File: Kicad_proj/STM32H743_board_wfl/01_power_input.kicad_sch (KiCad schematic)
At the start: 5 parts

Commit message: v0.4 poprawki inputa zasilania
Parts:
- removed C6: 47uF, symbol Device:C
- removed C7: 1uF, symbol Device:C
- removed C8: 100nF, symbol Device:C
- removed L2: BLM21PG221SN1D, symbol Device:L_Ferrite
- added C1, C2: 47uF, Capacitor_SMD:C_1206_3216Metric, symbol Device:C
- added C3: 1uF, Capacitor_SMD:C_0603_1608Metric, symbol Device:C
- added C4: 100nF, Capacitor_SMD:C_01005_0402Metric, symbol Device:C
- added F2: 1A Fuse 0680L1000-05, STM32H743_board_library_footprints:FUSC6125X279N, symbol STM32H743_board_library_symbols:0680L1000-05
- D1: footprint (none) -> Diode_SMD:D_SMB
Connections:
- net +BATT: now also F2.1; no longer D1.2 (A2)
- net -BATT: now also C1.2, C2.2, C3.2, C4.2
- new net +26V_prefiltered: C1.1, C2.1, C3.1, C4.1, D1.2 (A2), F2.2

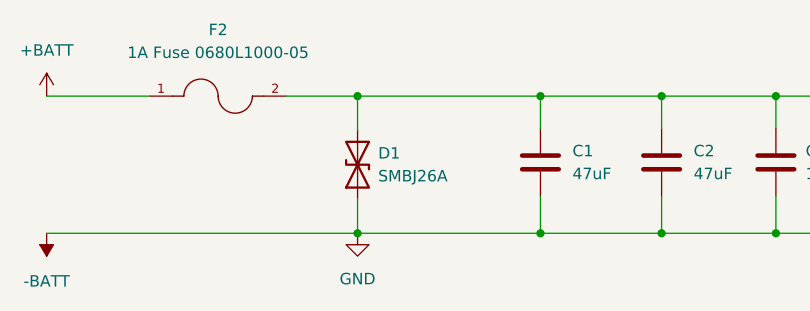
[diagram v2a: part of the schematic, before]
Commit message: v0.5b tvs and stm32 vbat fixes
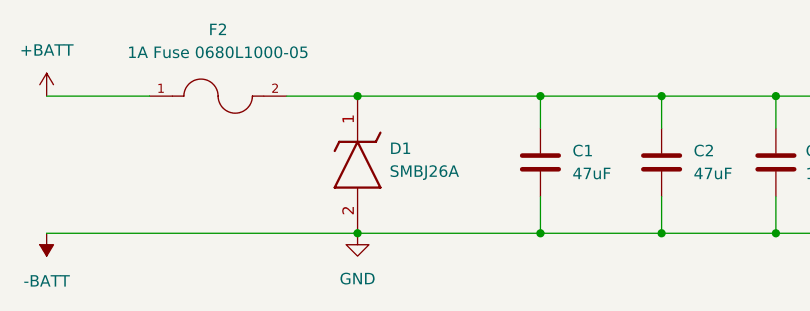
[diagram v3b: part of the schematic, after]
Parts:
- D1: symbol Device:D_TVS -> STM32H743_board_library_symbols:SMBJ26A; Height (none) -> 2.44; Manufacturer_Name (none) -> Vishay; Manufacturer_Part_Number (none) -> SMBJ5.0A-E3/5B
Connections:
- net +26V_prefiltered: now also D1.1 (K); no longer D1.2 (A2)
- net -BATT: now also D1.2 (A); no longer D1.1 (A1)

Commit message: PCB v0.1b connectors
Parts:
- renumbered F2 to F1
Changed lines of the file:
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@@
 		(dnp no)
 		(fields_autoplaced yes)
-		(property "Reference" "F2"
-			(at 101.854 78.486 0)
+		(property "Reference" "F1"
+			(at 101.854 78.74 0)
 			(show_name no)
 			(do_not_autoplace no)
@@
 		)
 		(property "Value" "1A Fuse 0680L1000-05"
-			(at 101.854 81.026 0)
+			(at 101.854 81.28 0)
 			(show_name no)
 			(do_not_autoplace no)
@@
 			(project "STM32H743_board_wfl"
 				(path "/3ffbaf01-8fe7-4f96-b685-21b9df9d548a/81f7828a-9cc3-44cb-b1b6-c28345015d19"
-					(reference "F2")
+					(reference "F1")
 					(unit 1)
 				)

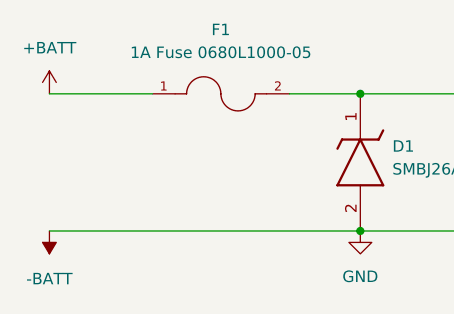
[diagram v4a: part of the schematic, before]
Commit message: PCB v0.1d components placement STM32 caps
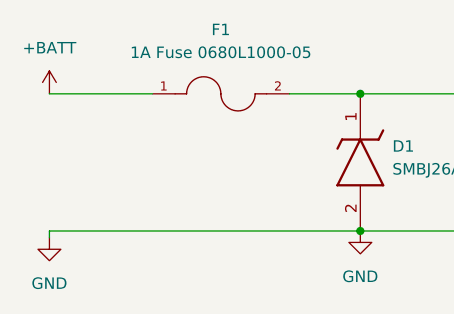
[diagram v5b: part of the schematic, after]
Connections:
- net -BATT renamed GND
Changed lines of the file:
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@@
+	(wire
+		(pts
+			(xy 82.804 101.092) (xy 82.804 101.854)
+		)
+		(stroke
+			(width 0)
+			(type default)
+		)
+	)
 	(wire
 		(pts
@@
 		(dnp no)
 		(fields_autoplaced yes)
-		(property "Reference" "#PWR04"
+		(property "Reference" "#PWR03"
 			(at 117.348 107.442 0)
 			(hide yes)
@@
 		(property "Description" "Power symbol creates a global label with name \"GND\" , ground"
 			(at 117.348 101.092 0)
-			(hide yes)
-			(show_name no)
-			(do_not_autoplace no)
-			(effects
-				(font
-					(size 1.27 1.27)
-				)
-			)
-		)
-		(pin "1"
-		)
-		(instances
-			(project "STM32H743_board_wfl"
-				(path "/3ffbaf01-8fe7-4f96-b685-21b9df9d548a/81f7828a-9cc3-44cb-b1b6-c28345015d19"
-					(reference "#PWR04")
-					(unit 1)
-				)
-			)
-		)
-	)
-	(symbol
-		(lib_id "power:-BATT")
-		(at 82.804 101.092 180)
-		(unit 1)
-		(body_style 1)
-		(exclude_from_sim no)
-		(in_bom yes)
-		(on_board yes)
-		(in_pos_files yes)
-		(dnp no)
-		(fields_autoplaced yes)
-		(property "Reference" "#PWR03"
-			(at 82.804 97.282 0)
-			(hide yes)
-			(show_name no)
-			(do_not_autoplace no)
-			(effects
-				(font
-					(size 1.27 1.27)
-				)
-			)
-		)
-		(property "Value" "-BATT"
-			(at 82.804 106.426 0)
-			(show_name no)
-			(do_not_autoplace no)
-			(effects
-				(font
-					(size 1.27 1.27)
-				)
-			)
-		)
-		(property "Footprint" ""
-			(at 82.804 101.092 0)
-			(hide yes)
-			(show_name no)
-			(do_not_autoplace no)
-			(effects
-				(font
-					(size 1.27 1.27)
-				)
-			)
-		)
-		(property "Datasheet" ""
-			(at 82.804 101.092 0)
-			(hide yes)
-			(show_name no)
-			(do_not_autoplace no)
-			(effects
-				(font
-					(size 1.27 1.27)
-				)
-			)
-		)
-		(property "Description" "Power symbol creates a global label with name \"-BATT\""
-			(at 82.804 101.092 0)
 			(hide yes)
 			(show_name no)
@@
 		(dnp no)
 		(fields_autoplaced yes)
-		(property "Reference" "#PWR05"
+		(property "Reference" "#PWR04"
 			(at 203.2 107.442 0)
 			(hide yes)
@@
 			(hide yes)
 			(show_name no)
+			(do_not_autoplace no)
+			(effects
+				(font
+					(size 1.27 1.27)
+				)
+			)
+		)
+		(pin "1"
+		)
+		(instances
+			(project "STM32H743_board_wfl"
+				(path "/3ffbaf01-8fe7-4f96-b685-21b9df9d548a/81f7828a-9cc3-44cb-b1b6-c28345015d19"
+					(reference "#PWR04")
+					(unit 1)
+				)
+			)
+		)
+	)
+	(symbol
+		(lib_id "power:GND")
+		(at 82.804 101.854 0)
+		(unit 1)
+		(body_style 1)
+		(exclude_from_sim no)
+		(in_bom yes)
+		(on_board yes)
+		(in_pos_files yes)
+		(dnp no)
+		(fields_autoplaced yes)
+		(property "Reference" "#PWR05"
+			(at 82.804 108.204 0)
+			(hide yes)
+			(show_name no)
+			(do_not_autoplace no)
+			(effects
+				(font
+					(size 1.27 1.27)
+				)
+			)
+		)
+		(property "Value" "GND"
+			(at 82.804 106.934 0)
+			(show_name no)
+			(do_not_autoplace no)
+			(effects
+				(font
+					(size 1.27 1.27)
+				)
+			)
+		)
+		(property "Footprint" ""
+			(at 82.804 101.854 0)
+			(hide yes)
+			(show_name no)
+			(do_not_autoplace no)
+			(effects
+				(font
+					(size 1.27 1.27)
+				)
+			)
+		)
+		(property "Datasheet" ""
+			(at 82.804 101.854 0)
+			(hide yes)
+			(show_name no)
+			(do_not_autoplace no)
+			(effects
+				(font
+					(size 1.27 1.27)
+				)
+			)
+		)
+		(property "Description" "Power symbol creates a global label with name \"GND\" , ground"
+			(at 82.804 101.854 0)
+			(hide yes)
+			(show_name no)
